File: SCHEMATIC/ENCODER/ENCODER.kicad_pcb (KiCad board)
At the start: 2 copper layers, 28 x 28 mm, 13 parts, among them J1 Analog OUT, J2 I2C OUT, SW1 mode sel, U1 magnetic_encoder_AS5600

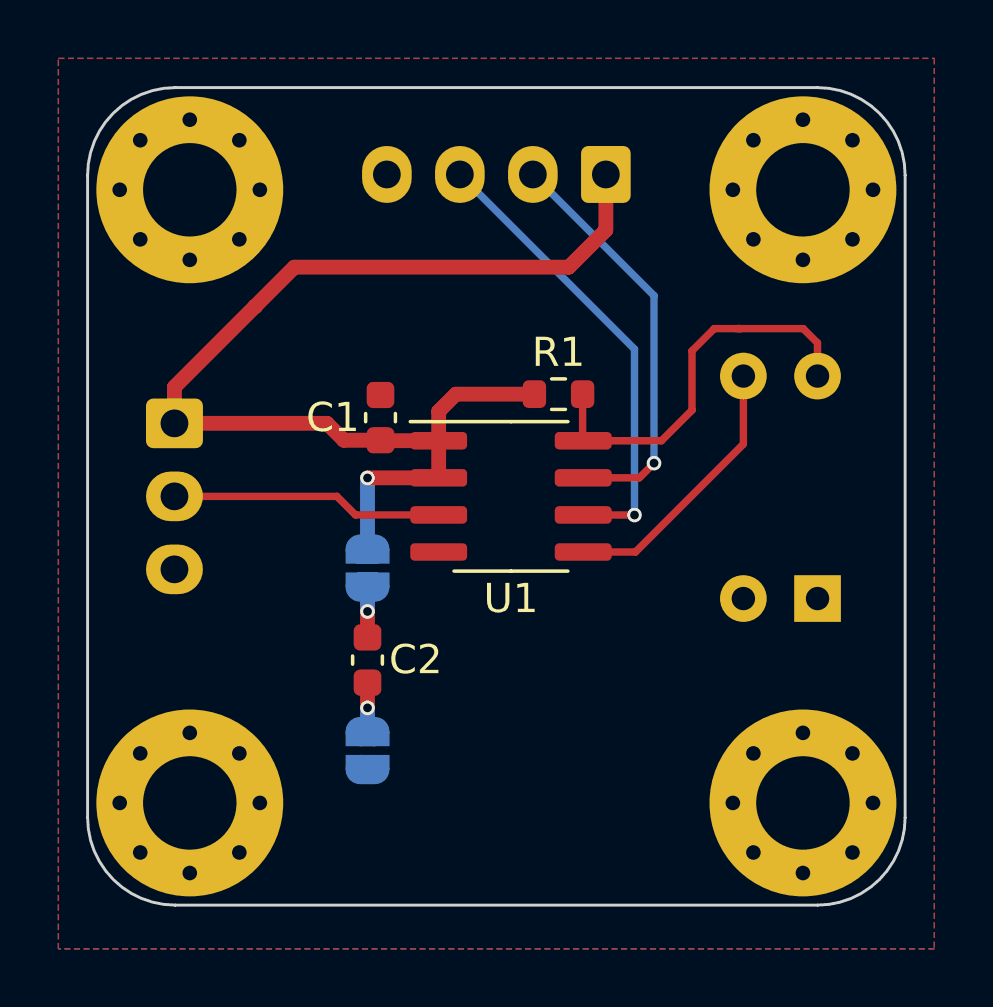
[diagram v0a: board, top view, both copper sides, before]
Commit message: Aggiunto Modello 3d case ENCODER
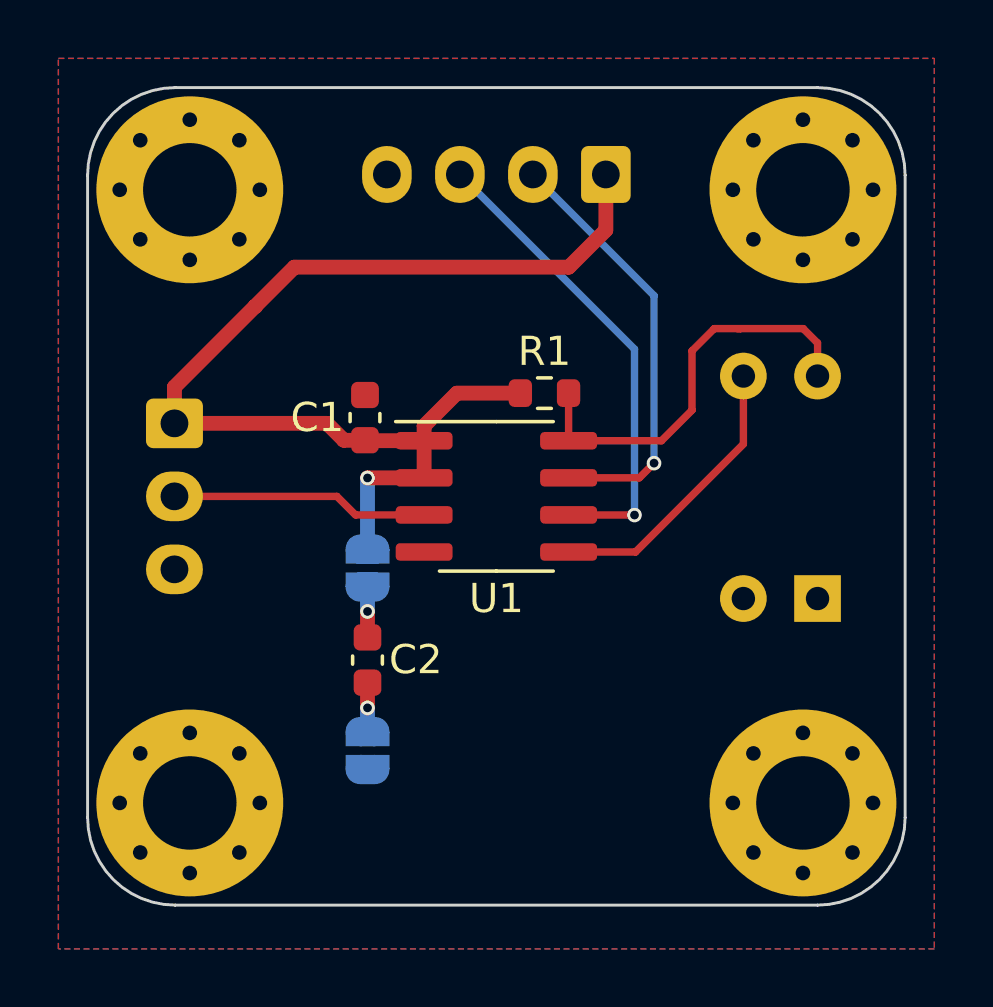
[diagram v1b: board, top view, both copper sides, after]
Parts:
- moved C1 0.53 mm to (119.5, 91.3)
- moved U1 0.50 mm to (124.0, 94.0)
- moved R1 0.48 mm to (125.6, 90.5)
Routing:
- net +3V3: track 40.2 -> 38.9 mm
- net /SCL: track 14.3 -> 15.3 mm
- net /DIR: track 13.9 -> 14.4 mm
- net /PGO: track 9.35 -> 9.85 mm
- net /OUT: track 9.31 -> 8.81 mm
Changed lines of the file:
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@@
     (48 "B.Fab" user)
     (49 "F.Fab" user)
+    (50 "User.1" user "costruzione")
   )
   (setup
@@
     )
     (pad_to_mask_clearance 0)
-    (grid_origin 122 92.1)
+    (grid_origin 110 80)
     (pcbplotparams
       (layerselection 0x00010fc_ffffffff)
@@
   )
   (footprint "Capacitor_SMD:C_0603_1608Metric" (layer "F.Cu")
-    (at 120.033 91.303 90)
+    (at 119.5 91.303 90)
     (descr "Capacitor SMD 0603 (1608 Metric), square (rectangular) end terminal, IPC_7351 nominal, (Body size source: IPC-SM-782 page 76, https://www.pcb-3d.com/wordpress/wp-content/uploads/ipc-sm-782a_amendment_1_and_2.pdf), generated with kicad-footprint-generator")
     (tags "capacitor")
@@
   )
   (footprint "Package_SO:SOIC-8_3.9x4.9mm_P1.27mm" (layer "F.Cu")
-    (at 124.5 94)
+    (at 124 94)
     (descr "SOIC, 8 Pin (JEDEC MS-012AA, https://www.analog.com/media/en/package-pcb-resources/package/pkg_pdf/soic_narrow-r/r_8.pdf), generated with kicad-footprint-generator ipc_gullwing_generator.py")
     (tags "SOIC SO")
@@
   )
   (footprint "Resistor_SMD:R_0603_1608Metric" (layer "F.Cu")
-    (at 126.129 90.5)
+    (at 125.6464 90.4648)
     (descr "Resistor SMD 0603 (1608 Metric), square (rectangular) end terminal, IPC_7351 nominal, (Body size source: IPC-SM-782 page 72, https://www.pcb-3d.com/wordpress/wp-content/uploads/ipc-sm-782a_amendment_1_and_2.pdf), generated with kicad-footprint-generator")
     (tags "resistor")
@@
   (gr_line (start 110 83) (end 110 105) (layer "Edge.Cuts") (width 0.1))
   (gr_line (start 113 108) (end 135 108) (layer "Edge.Cuts") (width 0.1))
+  (gr_line (start 110 80) (end 138 108) (layer "User.1") (width 0.02))
+  (gr_line (start 138 80) (end 110 108) (layer "User.1") (width 0.02))
   (gr_text "CONNECT FOR OTP\nPROGRAMMING" (at 126.064 102.641) (layer "B.SilkS")
     (effects (font (size 0.7 0.7) (thickness 0.15)) (justify mirror))
@@
     (effects (font (size 1 1) (thickness 0.15)) (justify mirror))
   )
+  (segment (start 119.592 93.365) (end 121.525 93.365) (width 0.508) (layer "F.Cu") (net 1))
   (segment (start 112.975 90.257) (end 112.975 91.5) (width 0.508) (layer "F.Cu") (net 1))
-  (segment (start 122.614 90.5) (end 122.025 91.089) (width 0.508) (layer "F.Cu") (net 1))
-  (segment (start 118.776 92.078) (end 120.033 92.078) (width 0.508) (layer "F.Cu") (net 1))
+  (segment (start 112.975 91.5) (end 118.198 91.5) (width 0.508) (layer "F.Cu") (net 1))
+  (segment (start 121.525 92.095) (end 119.517 92.095) (width 0.508) (layer "F.Cu") (net 1))
+  (segment (start 118.776 92.078) (end 119.5 92.078) (width 0.508) (layer "F.Cu") (net 1))
+  (segment (start 122.6492 90.4648) (end 121.525 91.589) (width 0.508) (layer "F.Cu") (net 1))
   (segment (start 127.75 82.975) (end 127.75 84.88) (width 0.508) (layer "F.Cu") (net 1))
-  (segment (start 122.025 91.089) (end 122.025 92.095) (width 0.508) (layer "F.Cu") (net 1))
   (segment (start 115.75 87.5) (end 115.741 87.491) (width 0.508) (layer "F.Cu") (net 1))
-  (segment (start 120.05 92.095) (end 120.033 92.078) (width 0.508) (layer "F.Cu") (net 1))
   (segment (start 127.75 82.975) (end 127.78 83.005) (width 0.508) (layer "F.Cu") (net 1))
+  (segment (start 127.75 84.88) (end 126.48 86.15) (width 0.508) (layer "F.Cu") (net 1))
+  (segment (start 121.525 91.589) (end 121.525 92.095) (width 0.508) (layer "F.Cu") (net 1))
+  (segment (start 121.525 93.365) (end 121.525 92.095) (width 0.508) (layer "F.Cu") (net 1))
   (segment (start 118.198 91.5) (end 118.776 92.078) (width 0.508) (layer "F.Cu") (net 1))
-  (segment (start 127.75 84.88) (end 126.48 86.15) (width 0.508) (layer "F.Cu") (net 1))
-  (segment (start 122.025 92.095) (end 120.05 92.095) (width 0.508) (layer "F.Cu") (net 1))
   (segment (start 117.082 86.15) (end 115.741 87.491) (width 0.508) (layer "F.Cu") (net 1))
-  (segment (start 122.025 93.365) (end 122.025 92.095) (width 0.508) (layer "F.Cu") (net 1))
+  (segment (start 124.8214 90.4648) (end 122.6492 90.4648) (width 0.508) (layer "F.Cu") (net 1))
   (segment (start 119.587 93.37) (end 119.592 93.365) (width 0.508) (layer "F.Cu") (net 1))
-  (segment (start 125.304 90.5) (end 122.614 90.5) (width 0.508) (layer "F.Cu") (net 1))
-  (segment (start 119.592 93.365) (end 122.025 93.365) (width 0.508) (layer "F.Cu") (net 1))
+  (segment (start 119.517 92.095) (end 119.5 92.078) (width 0.508) (layer "F.Cu") (net 1))
   (segment (start 115.741 87.491) (end 112.975 90.257) (width 0.508) (layer "F.Cu") (net 1))
-  (segment (start 112.975 91.5) (end 118.198 91.5) (width 0.508) (layer "F.Cu") (net 1))
   (segment (start 126.48 86.15) (end 117.082 86.15) (width 0.508) (layer "F.Cu") (net 1))
   (via (at 119.587 93.37) (size 0.5) (drill 0.3) (layers "F.Cu" "B.Cu") (net 1))
   (segment (start 119.587 93.37) (end 119.587 95.806) (width 0.508) (layer "B.Cu") (net 1))
   (segment (start 115.75 87.5) (end 115.741 87.491) (width 0.508) (layer "B.Cu") (net 1))
-  (segment (start 122.025 94.635) (end 119.174 94.635) (width 0.254) (layer "F.Cu") (net 3))
+  (segment (start 121.525 94.635) (end 119.174 94.635) (width 0.254) (layer "F.Cu") (net 3))
+  (segment (start 118.539 94) (end 112.975 94) (width 0.254) (layer "F.Cu") (net 3))
   (segment (start 119.174 94.635) (end 118.539 94) (width 0.254) (layer "F.Cu") (net 3))
-  (segment (start 118.539 94) (end 112.975 94) (width 0.254) (layer "F.Cu") (net 3))
+  (segment (start 129.4 92.862) (end 128.897 93.365) (width 0.254) (layer "F.Cu") (net 4))
   (segment (start 127.01 93.4) (end 126.975 93.365) (width 0.254) (layer "F.Cu") (net 4))
-  (segment (start 128.897 93.365) (end 126.975 93.365) (width 0.254) (layer "F.Cu") (net 4))
-  (segment (start 129.4 92.862) (end 128.897 93.365) (width 0.254) (layer "F.Cu") (net 4))
+  (segment (start 128.897 93.365) (end 126.475 93.365) (width 0.254) (layer "F.Cu") (net 4))
+  (segment (start 126.975 93.365) (end 126.475 93.365) (width 0.254) (layer "F.Cu") (net 4))
   (via (at 129.4 92.862) (size 0.5) (drill 0.3) (layers "F.Cu" "B.Cu") (net 4))
   (segment (start 129.4 87.125) (end 125.25 82.975) (width 0.254) (layer "B.Cu") (net 4))
   (segment (start 129.4 92.862) (end 129.4 87.125) (width 0.254) (layer "B.Cu") (net 4))
-  (segment (start 128.731 94.64) (end 126.98 94.64) (width 0.254) (layer "F.Cu") (net 5))
-  (segment (start 126.98 94.64) (end 126.975 94.635) (width 0.254) (layer "F.Cu") (net 5))
+  (segment (start 126.48 94.64) (end 126.475 94.635) (width 0.254) (layer "F.Cu") (net 5))
+  (segment (start 128.731 94.64) (end 126.48 94.64) (width 0.254) (layer "F.Cu") (net 5))
   (via (at 128.731 94.64) (size 0.5) (drill 0.3) (layers "F.Cu" "B.Cu") (net 5))
   (segment (start 128.731 94.64) (end 128.731 88.956) (width 0.254) (layer "B.Cu") (net 5))
   (segment (start 128.731 88.956) (end 122.75 82.975) (width 0.254) (layer "B.Cu") (net 5))
-  (segment (start 129.655 92.095) (end 126.975 92.095) (width 0.254) (layer "F.Cu") (net 6))
+  (segment (start 126.4714 90.4648) (end 126.475 90.4684) (width 0.254) (layer "F.Cu") (net 6))
   (segment (start 130.701 91.049) (end 129.655 92.095) (width 0.254) (layer "F.Cu") (net 6))
+  (segment (start 132.352 88.255) (end 131.463 88.255) (width 0.254) (layer "F.Cu") (net 6))
+  (segment (start 129.655 92.095) (end 126.475 92.095) (width 0.254) (layer "F.Cu") (net 6))
+  (segment (start 134.511 88.255) (end 132.352 88.255) (width 0.254) (layer "F.Cu") (net 6))
+  (segment (start 126.475 90.4684) (end 126.475 92.095) (width 0.254) (layer "F.Cu") (net 6))
   (segment (start 130.701 89.017) (end 130.701 91.049) (width 0.254) (layer "F.Cu") (net 6))
-  (segment (start 131.463 88.255) (end 130.701 89.017) (width 0.254) (layer "F.Cu") (net 6))
-  (segment (start 132.352 88.255) (end 131.463 88.255) (width 0.254) (layer "F.Cu") (net 6))
-  (segment (start 126.954 92.074) (end 126.975 92.095) (width 0.254) (layer "F.Cu") (net 6))
-  (segment (start 126.954 90.5) (end 126.954 92.074) (width 0.254) (layer "F.Cu") (net 6))
-  (segment (start 134.511 88.255) (end 132.352 88.255) (width 0.254) (layer "F.Cu") (net 6))
   (segment (start 135 88.744) (end 134.511 88.255) (width 0.254) (layer "F.Cu") (net 6))
   (segment (start 135 89.88) (end 135 88.744) (width 0.254) (layer "F.Cu") (net 6))
+  (segment (start 131.463 88.255) (end 130.701 89.017) (width 0.254) (layer "F.Cu") (net 6))
   (segment (start 132.352 88.255) (end 132.225 88.255) (width 0.254) (layer "F.Cu") (net 6))
   (segment (start 132.46 92.211) (end 132.46 89.88) (width 0.254) (layer "F.Cu") (net 7))
-  (segment (start 126.975 95.905) (end 128.766 95.905) (width 0.254) (layer "F.Cu") (net 7))
+  (segment (start 126.475 95.905) (end 128.766 95.905) (width 0.254) (layer "F.Cu") (net 7))
   (segment (start 128.766 95.905) (end 132.46 92.211) (width 0.254) (layer "F.Cu") (net 7))
   (segment (start 119.587 97.942) (end 119.587 98.831) (width 0.508) (layer "F.Cu") (net 8))
@@
     (polygon
       (pts
-        (xy 125.7592 91.084)
-        (xy 125.7084 95.7068)
-        (xy 125.4798 95.7068)
-        (xy 125.4798 91.6428)
-        (xy 123.524 91.6428)
-        (xy 123.524 95.656)
-        (xy 123.2192 95.656)
-        (xy 123.2192 91.084)
+        (xy 125.2592 91.084)
+        (xy 125.2084 95.7068)
+        (xy 124.9798 95.7068)
+        (xy 124.9798 91.6428)
+        (xy 123.024 91.6428)
+        (xy 123.024 95.656)
+        (xy 122.7192 95.656)
+        (xy 122.7192 91.084)
       )
     )

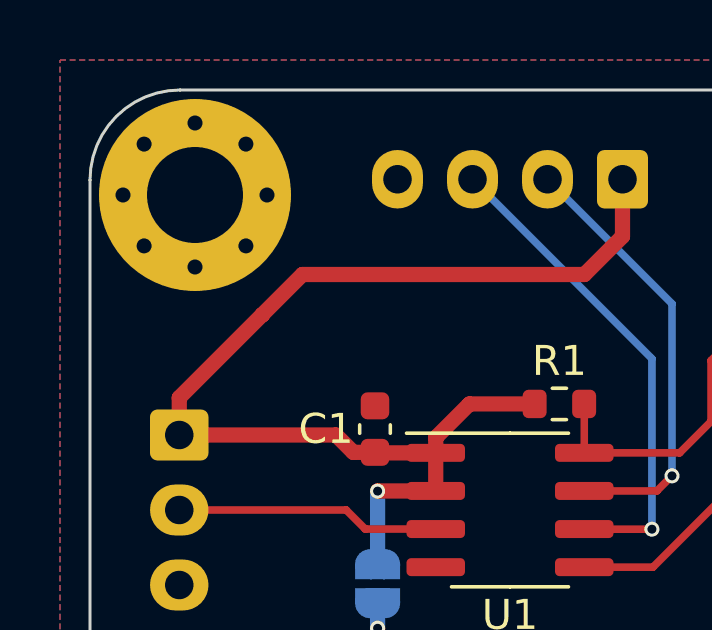
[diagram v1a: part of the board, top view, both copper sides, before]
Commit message: iniziato il layout, posizionati componenti principali
incominciato il posizionamento dei componenti nel layout. Sono stati posizionati i componenti principali come led RGB, GPS, schermo, pulsanti vari, buzzer
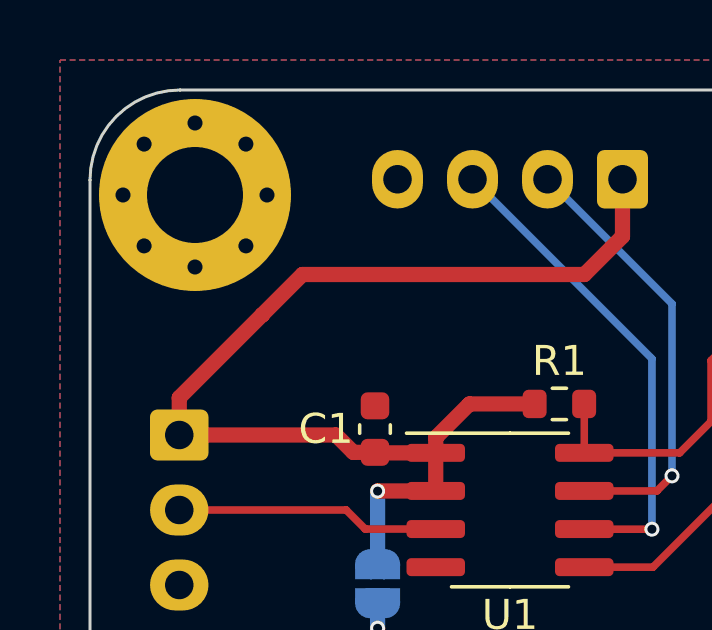
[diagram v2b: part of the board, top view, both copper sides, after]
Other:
- board text removed: "OTP"
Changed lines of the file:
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@@
-    (effects (font (size 1 1) (thickness 0.15)) (justify mirror))
-  )
-  (gr_text "OTP" (at 124 85.8) (layer "B.SilkS")
     (effects (font (size 1 1) (thickness 0.15)) (justify mirror))
   )
@@
   (gr_text "CCW" (at 125.5 98) (layer "B.SilkS")
     (effects (font (size 0.7 0.7) (thickness 0.15)) (justify left mirror))
-  )
-  (gr_text "OTP" (at 117.7 85.8) (layer "B.SilkS")
-    (effects (font (size 1 1) (thickness 0.15)) (justify mirror))
   )
   (gr_text "ANALOG OUT" (at 117.5 94 90) (layer "B.SilkS")
@@
   (via (at 119.587 93.37) (size 0.5) (drill 0.3) (layers "F.Cu" "B.Cu") (net 1))
   (segment (start 119.587 93.37) (end 119.587 95.806) (width 0.508) (layer "B.Cu") (net 1))
-  (segment (start 115.75 87.5) (end 115.741 87.491) (width 0.508) (layer "B.Cu") (net 1))
   (segment (start 121.525 94.635) (end 119.174 94.635) (width 0.254) (layer "F.Cu") (net 3))
   (segment (start 118.539 94) (end 112.975 94) (width 0.254) (layer "F.Cu") (net 3))

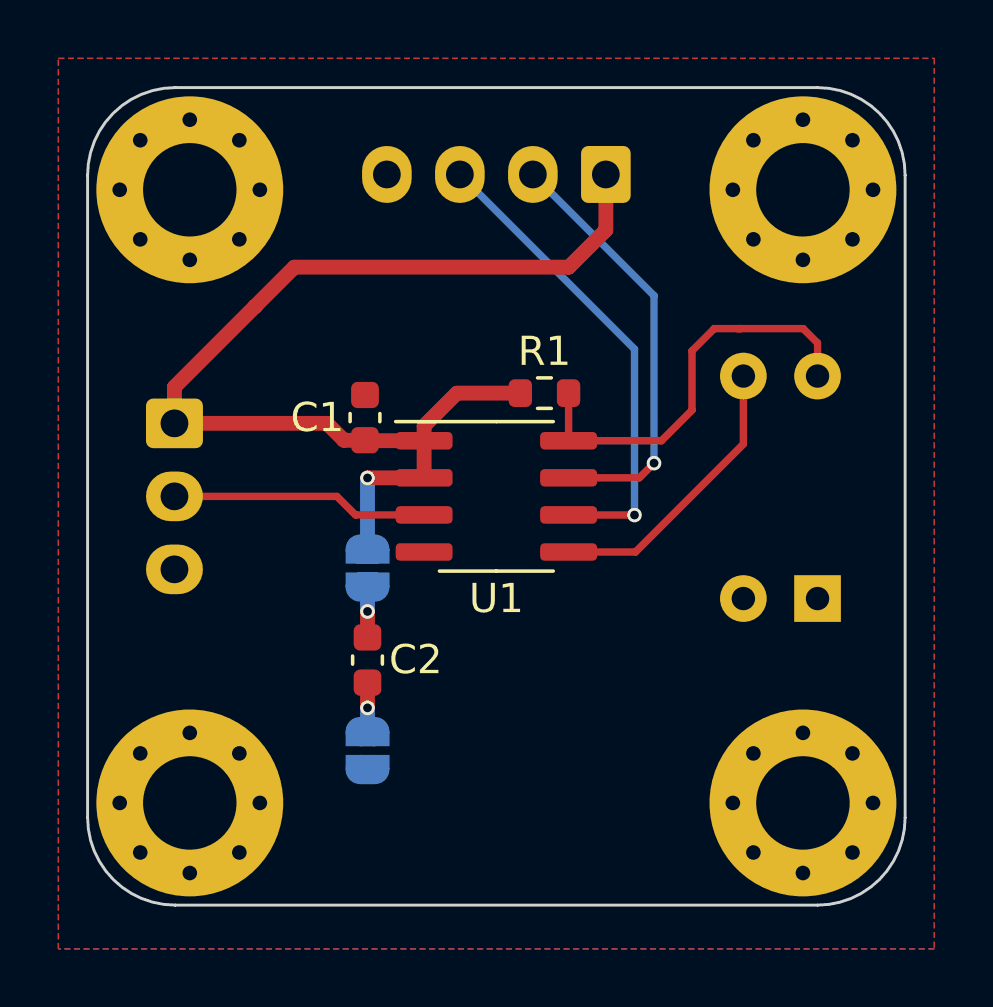
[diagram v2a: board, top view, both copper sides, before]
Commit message: iniziato lo broglio. Prima di continuare modificare pin schema
iniziato lo sbroglio della scheda, prima di continuare bisogna sistemare i pin che siano concordi con quelli degli altro (ovvero sistemarli come da tabella su telegram)
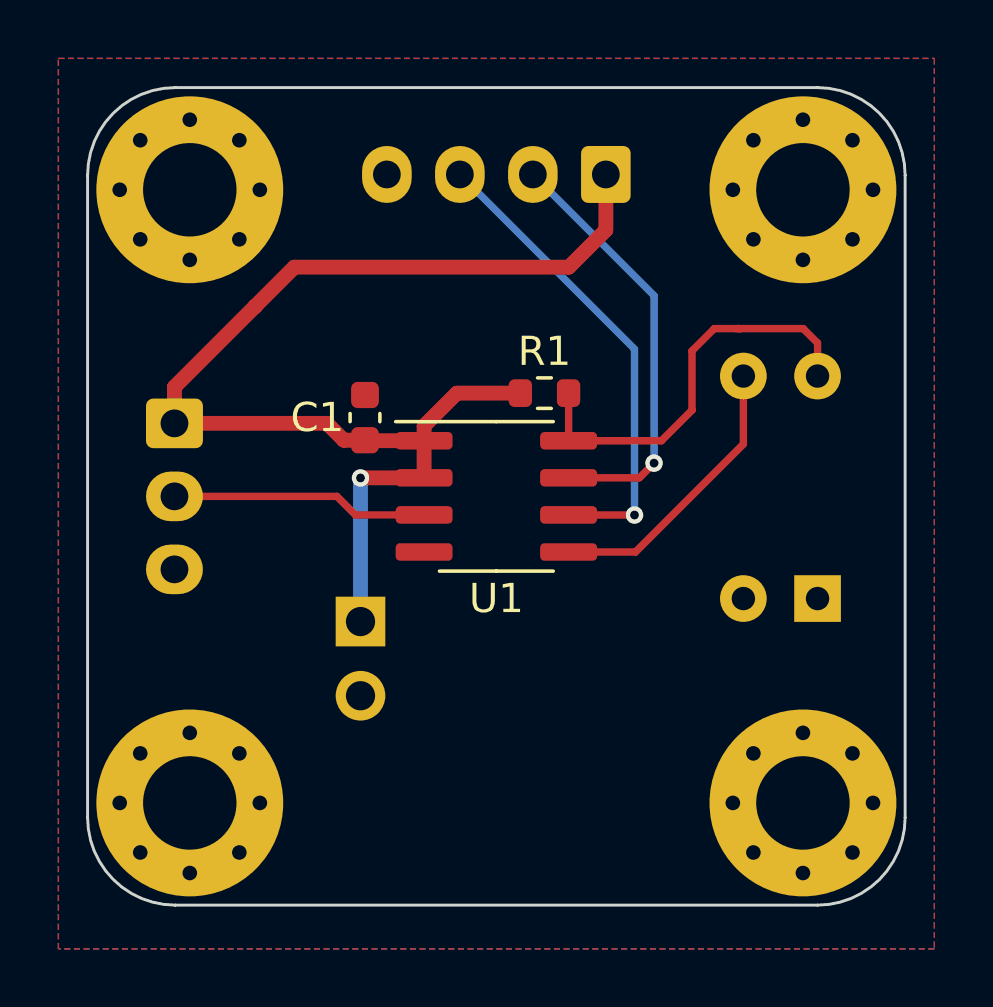
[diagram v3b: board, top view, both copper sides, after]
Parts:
- removed JP1, JP2: OTP only, Jumper:SolderJumper-2_P1.3mm_Open_RoundedPad1.0x1.5mm
- C2: footprint Capacitor_SMD:C_0603_1608Metric -> Connector_PinSocket_2.54mm:PinSocket_1x02_P2.54mm_Vertical; moved to B.Cu
- moved C2 1.34 mm to (119.3, 98.3), turned to 180 degrees
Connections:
- C2 pad 1: Net-(C2-Pad1) -> +3V3
- C2 pad 2: Net-(C2-Pad2) -> GND
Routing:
- net +3V3: track 38.9 -> 41.6 mm
- net Net-(C2-Pad1): track 1.73 -> 0.00 mm, vias 1 -> 0
- net Net-(C2-Pad2): track 1.67 -> 0.00 mm, vias 1 -> 0
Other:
- board text added: "CONNECT FOR OTP PROGRAMMING [10uF]"
- board text removed: "CONNECT FOR OTP PROGRAMMING"
